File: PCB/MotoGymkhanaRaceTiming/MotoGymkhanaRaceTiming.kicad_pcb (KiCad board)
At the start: 2 copper layers, 27 parts, among them U1 LM2577T-ADJ_NOPB, U2 PC817, U3 PC817

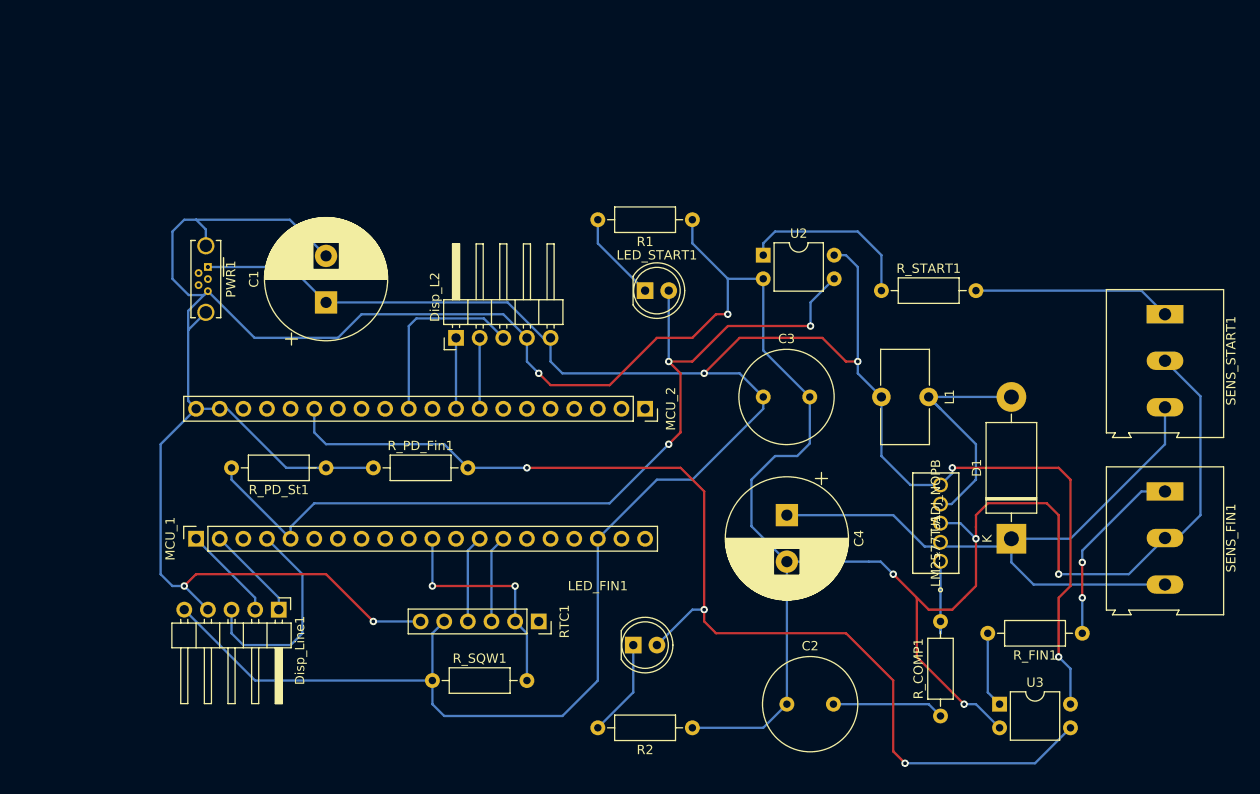
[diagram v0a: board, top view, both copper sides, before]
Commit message: Better PCB, now with jumpers (or headers to wire switches to) for configuration
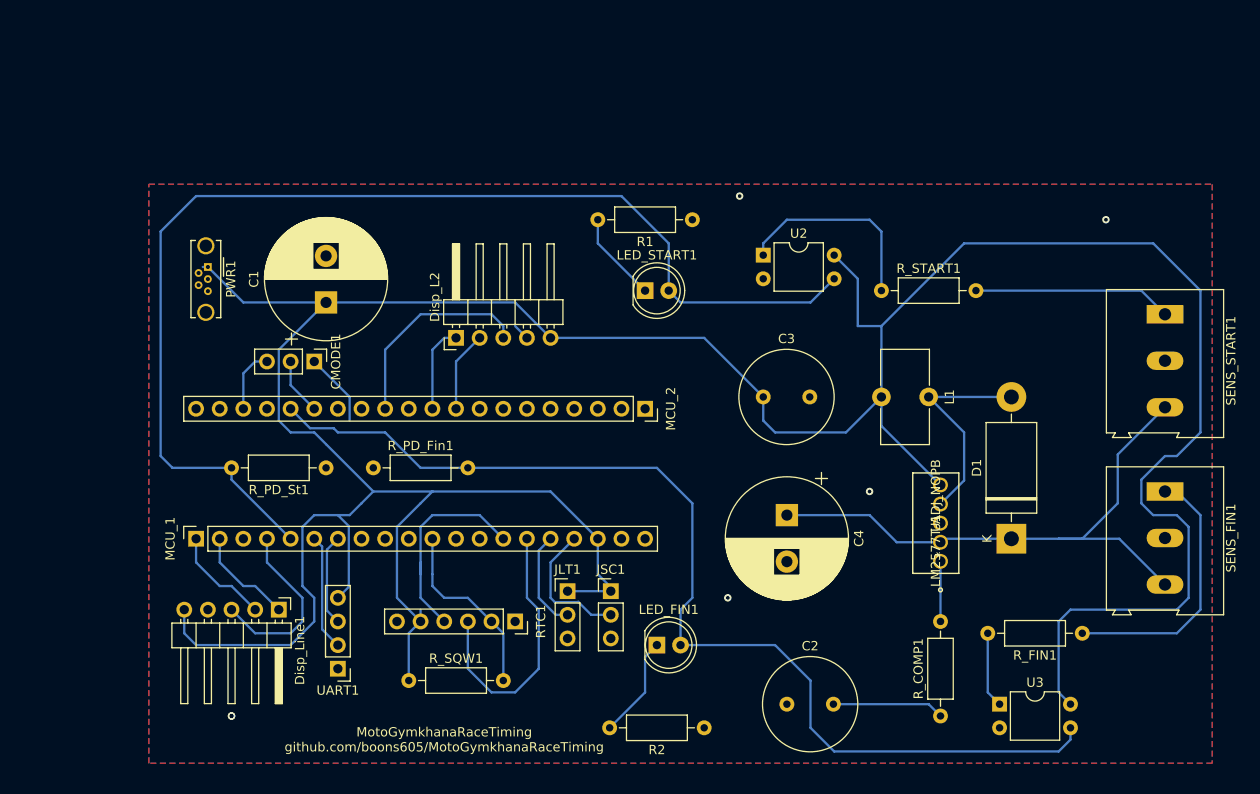
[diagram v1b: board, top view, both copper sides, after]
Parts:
- added CMODE1: Conn_01x03_Male, Connector_PinHeader_2.54mm:PinHeader_1x03_P2.54mm_Vertical, F.Cu at (132.1, 96.5)
- added JLT1: Conn_01x03_Male, Connector_PinHeader_2.54mm:PinHeader_1x03_P2.54mm_Vertical, F.Cu at (159.3, 121.2)
- added JSC1: Conn_01x03_Male, Connector_PinHeader_2.54mm:PinHeader_1x03_P2.54mm_Vertical, F.Cu at (164.0, 121.2)
- added UART1: Conn_01x04_Male, Connector_PinHeader_2.54mm:PinHeader_1x04_P2.54mm_Vertical, F.Cu at (134.6, 129.5)
- moved RTC1 2.54 mm to (153.7, 124.5)
- moved LED_FIN1 2.54 mm to (168.9, 127.0)
- moved R_SQW1 2.54 mm to (142.2, 130.8)
- moved R2 1.27 mm to (174.0, 135.9)
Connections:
- MCU_1 pad 19: Net-(MCU_1-Pad19) -> Net-(C1-Pad2)
- MCU_2 pad 10: Net-(MCU_2-Pad10) -> Net-(Disp_L2-Pad1)
- MCU_2 pad 11: Net-(Disp_L2-Pad3) -> Net-(MCU_2-Pad11)
- MCU_2 pad 12: Net-(MCU_2-Pad12) -> Net-(Disp_L2-Pad3)
- MCU_2 pad 15: Net-(LED_FIN1-Pad2) -> Net-(CMODE1-Pad2)
- MCU_2 pad 16: Net-(MCU_2-Pad16) -> Net-(LED_FIN1-Pad2)
- MCU_2 pad 8: Net-(Disp_L2-Pad2) -> Net-(MCU_2-Pad8)
- MCU_2 pad 9: Net-(Disp_L2-Pad1) -> Net-(Disp_L2-Pad2)
- RTC1 pad 3: Net-(MCU_1-Pad14) -> Net-(MCU_1-Pad15)
- RTC1 pad 4: Net-(MCU_1-Pad13) -> Net-(MCU_1-Pad14)
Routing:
- net Net-(C1-Pad2): track 377.3 -> 9.72 mm, vias 8 -> 6
- net Net-(C1-Pad1): track 258.2 -> 356.7 mm, vias 4 -> 0
- net Net-(MCU_1-Pad15): track 0.00 -> 29.3 mm
- net Net-(LED_START1-Pad2): track 96.4 -> 125.4 mm, vias 3 -> 0
- net Net-(JSC1-Pad2): track 0.00 -> 14.7 mm
- net Net-(MCU_1-Pad14): track 9.42 -> 23.0 mm
- net Net-(MCU_1-Pad6): track 0.00 -> 12.5 mm
- net Net-(JLT1-Pad2): track 0.00 -> 10.7 mm
- net Net-(MCU_1-Pad7): track 0.00 -> 9.86 mm
- net Net-(MCU_1-Pad13): track 9.42 -> 0.00 mm
- net Net-(R_FIN1-Pad1): track 20.4 -> 28.8 mm, vias 2 -> 0
- net Net-(CMODE1-Pad3): track 0.00 -> 6.88 mm
- net Net-(C4-Pad1): track 70.6 -> 64.4 mm
- net Net-(CMODE1-Pad2): track 0.00 -> 6.13 mm
- net Net-(LED_FIN1-Pad2): track 119.4 -> 114.6 mm, vias 3 -> 0
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- added copper zone on B.Cu, net Net-(C1-Pad2)
- added copper zone on F.Cu, net Net-(C1-Pad2)
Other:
- board text added: "MotoGymkhanaRaceTiming github.com/boons605/MotoGymkhanaRaceTiming"

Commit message: Updated PCB, added board outline
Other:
- board outline added: 116.8 x 64.8 mm
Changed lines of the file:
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@@
   (general
     (thickness 1.6)
-    (drawings 1)
+    (drawings 5)
     (tracks 215)
     (zones 0)
@@
       (effects (font (size 1 1) (thickness 0.15)))
     )
-    (fp_text value 0.33uF (at 2.5 6.25) (layer F.Fab)
+    (fp_text value 0.33uF (at -2.54 5.08) (layer F.Fab)
       (effects (font (size 1 1) (thickness 0.15)))
     )
@@
     (descr "Altech AK300 terminal block, pitch 5.0mm, 45 degree angled, see http://www.mouser.com/ds/2/16/PCBMETRC-24178.pdf")
     (tags "Altech AK300 terminal block pitch 5.0mm")
-    (fp_text reference SENS_FIN1 (at 5 -7.1 90) (layer F.SilkS)
+    (fp_text reference SENS_FIN1 (at 3.81 7.62 90) (layer F.SilkS)
       (effects (font (size 1 1) (thickness 0.15)))
     )
@@
     (descr "Altech AK300 terminal block, pitch 5.0mm, 45 degree angled, see http://www.mouser.com/ds/2/16/PCBMETRC-24178.pdf")
     (tags "Altech AK300 terminal block pitch 5.0mm")
-    (fp_text reference SENS_START1 (at 5 -7.1 90) (layer F.SilkS)
+    (fp_text reference SENS_START1 (at 3.81 7.62 90) (layer F.SilkS)
       (effects (font (size 1 1) (thickness 0.15)))
     )
@@
     )
   )
+  (gr_line (start 113.03 140.97) (end 113.03 76.2) (layer Edge.Cuts) (width 0.05))
+  (gr_line (start 229.87 140.97) (end 113.03 140.97) (layer Edge.Cuts) (width 0.05))
+  (gr_line (start 229.87 76.2) (end 229.87 140.97) (layer Edge.Cuts) (width 0.05))
+  (gr_line (start 113.03 76.2) (end 229.87 76.2) (layer Edge.Cuts) (width 0.05))
   (gr_text "MotoGymkhanaRaceTiming\ngithub.com/boons605/MotoGymkhanaRaceTiming" (at 146.05 137.16) (layer F.SilkS)
     (effects (font (size 1 1) (thickness 0.15)))

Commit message: PCB update
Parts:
- added Btn1: Conn_01x02_Male, Connector_PinHeader_2.54mm:PinHeader_1x02_P2.54mm_Vertical, F.Cu at (147.3, 76.2)
- added Btn2: Conn_01x02_Male, Connector_PinHeader_2.54mm:PinHeader_1x02_P2.54mm_Vertical, F.Cu at (151.1, 76.2)
- added H1: MountingHole_Pad, MountingHole:MountingHole_3.2mm_M3_Pad_Via, F.Cu at (194.3, 64.8)
- added H2: MountingHole_Pad, MountingHole:MountingHole_3.2mm_M3_Pad_Via, F.Cu at (194.3, 119.4)
- added H3: MountingHole_Pad, MountingHole:MountingHole_3.2mm_M3_Pad_Via, F.Cu at (105.4, 119.4)
- added H4: MountingHole_Pad, MountingHole:MountingHole_3.2mm_M3_Pad_Via, F.Cu at (105.4, 64.8)
- added R33: 33k, Resistor_THT:R_Axial_DIN0207_L6.3mm_D2.5mm_P10.16mm_Horizontal, F.Cu at (176.5, 109.2)
- added R39: 3k9, Resistor_THT:R_Axial_DIN0207_L6.3mm_D2.5mm_P10.16mm_Horizontal, F.Cu at (180.3, 99.1)
- added R_PD_B1: 10k, Resistor_THT:R_Axial_DIN0207_L6.3mm_D2.5mm_P10.16mm_Horizontal, F.Cu at (142.2, 88.9)
- added R_PD_B2: 10k, Resistor_THT:R_Axial_DIN0207_L6.3mm_D2.5mm_P10.16mm_Horizontal, F.Cu at (160.0, 81.3)
- C1: footprint Capacitor_THT:CP_Radial_D13.0mm_P5.00mm -> Capacitor_THT:CP_Radial_D8.0mm_P5.00mm
- C2, C3: footprint Capacitor_THT:C_Radial_D10.0mm_H12.5mm_P5.00mm -> Capacitor_THT:C_Disc_D4.7mm_W2.5mm_P5.00mm
- C4: footprint Capacitor_THT:CP_Radial_D13.0mm_P5.00mm -> Capacitor_THT:CP_Radial_D10.0mm_P5.00mm
- Disp_L2, Disp_Line1: footprint Connector_PinHeader_2.54mm:PinHeader_1x05_P2.54mm_Horizontal -> MotoGymkhanaRaceTiming:DisplayLineConnector
- L1: footprint Inductor_THT:L_Toroid_Vertical_L10.0mm_W5.0mm_P5.08mm -> Inductor_THT:L_Radial_D7.0mm_P3.00mm
- SENS_FIN1, SENS_START1: footprint TerminalBlock:TerminalBlock_Altech_AK300-3_P5.00mm -> MotoGymkhanaRaceTiming:SensorConnector
- U1: footprint footprints:LM2577T -> footprints:LM2577T-ADJ&slash_NOPB
- UART1: footprint Connector_PinHeader_2.54mm:PinHeader_1x04_P2.54mm_Vertical -> MotoGymkhanaRaceTiming:UART
- moved C4 38.1 mm to (182.9, 74.9), turned to 90 degrees
- moved D1 37.4 mm to (176.5, 94.0)
- moved SENS_FIN1 34.2 mm to (191.8, 97.8)
- moved R_START1 33.3 mm to (171.4, 63.5)
- moved SENS_START1 33.3 mm to (191.8, 81.3)
- moved L1 33.1 mm to (170.2, 82.5), turned to 180 degrees
- moved R_COMP1 30.7 mm to (175.3, 115.6), turned to 180 degrees
- moved U1 30.3 mm to (170.2, 109.2)
- moved U3 29.6 mm to (180.3, 118.1)
- moved C3 28.5 mm to (165.1, 76.2)
- moved R_FIN1 26.7 mm to (190.5, 114.3)
- moved Disp_L2 22.5 mm to (132.1, 77.5)
- moved U2 20.8 mm to (167.6, 68.6)
- moved R_PD_Fin1 20.8 mm to (125.7, 91.4)
- moved CMODE1 20.8 mm to (119.4, 80.0)
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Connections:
- RTC1 pad 3: Net-(MCU_1-Pad15) -> Net-(MCU_1-Pad14)
- RTC1 pad 4: Net-(MCU_1-Pad14) -> Net-(MCU_1-Pad15)
- U1 pad 2: Net-(C4-Pad1) -> Net-(R33-Pad1)
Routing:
- net Net-(Btn1-Pad1): track 6.88 -> 72.3 mm
- net Net-(Btn2-Pad2): track 0.00 -> 19.7 mm
- net Net-(C1-Pad1): track 356.7 -> 339.0 mm
- net Net-(R_START1-Pad1): track 21.9 -> 6.66 mm
- net Net-(LED_FIN1-Pad2): track 114.6 -> 99.9 mm
- net Net-(Btn1-Pad2): track 0.00 -> 13.8 mm
- net Net-(D1-Pad2): track 23.0 -> 35.3 mm
- net Net-(R33-Pad1): track 0.00 -> 10.7 mm
- net Net-(LED_START1-Pad2): track 125.4 -> 117.8 mm
- net Net-(R_FIN1-Pad1): track 28.8 -> 21.7 mm
- net Net-(C2-Pad2): track 12.0 -> 5.11 mm
- net Net-(MCU_1-Pad14): track 23.0 -> 29.3 mm
- net Net-(C4-Pad1): track 64.4 -> 58.4 mm
- net Net-(R_FIN1-Pad2): track 8.15 -> 3.81 mm
- net Net-(JLT1-Pad2): track 10.7 -> 14.5 mm
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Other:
- board size 116.8 x 64.8 mm -> 99.1 x 64.8 mm

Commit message: Update for issue #9
- Adding text to RTC socket
- Adding UART2
- Trace width for 5V net updated
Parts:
- added UART2: Conn_01x04_Male, MotoGymkhanaRaceTiming:UART, F.Cu at (141.0, 80.0)
- RTC1: footprint Connector_PinSocket_2.54mm:PinSocket_1x06_P2.54mm_Vertical -> MotoGymkhanaRaceTiming:RTC_Socket
- moved Disp_L2 5.08 mm to (127.0, 77.5)
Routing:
- net Net-(MCU_2-Pad8): track 0.00 -> 11.7 mm
- net Net-(MCU_2-Pad7): track 0.00 -> 8.15 mm
- net Net-(Btn1-Pad1): track 72.3 -> 80.2 mm
- net Net-(C1-Pad1): track 339.0 -> 344.4 mm
- net Net-(Disp_L2-Pad2): track 7.62 -> 9.72 mm
- net Net-(Disp_L2-Pad1): track 7.62 -> 9.72 mm
- net Net-(Disp_L2-Pad3): track 19.1 -> 17.3 mm
- net Net-(Btn1-Pad2): track 13.8 -> 12.3 mm
- net Net-(C4-Pad1): track 58.4 -> 59.0 mm
